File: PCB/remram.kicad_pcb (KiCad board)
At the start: 4 copper layers, 140 x 104 mm, 248 parts, among them J1 4DB-P108-06, J10 Conn_02x13_Odd_Even, J11 70543-0001, J12 70543-0002, J13 70543-0002, J14 70543-0002, J15 70543-0001, J16 70543-0002, J17 70543-0002, J18 70543-0002, J19 70543-0001, J2 039531-1002, J20 70543-0003, J21 70543-0003, J22 70543-0003, J23 70543-0003, J3 70543-0003, J4 67068-8000, J5 Conn_02x05, J6 Conn_02x05, J7 70543-0002, J8 70543-0002, J9 62201021121, Q1 PMV50EPEA, Q2 PSMN1R2-30YLC,115, Q3 BUK9840-55, Q4 PSMN1R2-30YLC,115, Q5 BUK9840-55, Q6 PMV50EPEA, SW1 OS102011MA1QN1, SW2 PTS645VL39-2, U1 TPS54308, U2 AP2112K-3.3TRG1, U3 ADUM4160, U4 STM32F765VIT6, U5 TMC2130-TA, U6 TMC2130-TA, U7 TMC2130-TA, U8 TMC2130-TA, Y1 TSX-3225 24.0000MF15X-AC3

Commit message: Made small cosmetic changes
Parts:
- added REF**: OSHW-Logo2_14.6x12mm_SilkScreen, Symbol:OSHW-Logo2_14.6x12mm_SilkScreen, F.Cu at (69.5, 76.2)
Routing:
- net /MCU/PWM_HEAT: track 76.3 -> 74.3 mm

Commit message: Fix minor cosmetic issues
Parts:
- moved C14 7.55 mm to (177.7, 93.8)
- moved C13 5.45 mm to (184.2, 92.8)
- moved D4 0.40 mm to (175.2, 118.0)
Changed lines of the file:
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@@
   (module custom-footprints:S8401-46 (layer F.Cu)
     (at 140.6 101 90)
-    (fp_text reference BT1 (at 0 4 90) (layer F.SilkS)
+    (fp_text reference BT1 (at 12.55 0 180) (layer F.SilkS)
       (effects (font (size 1 1) (thickness 0.15)))
     )
@@
     (tags capacitor)
     (attr smd)
-    (fp_text reference C22 (at -3.082727 -0.640025 180) (layer F.SilkS)
+    (fp_text reference C22 (at -2.782727 0.009975 180) (layer F.SilkS)
       (effects (font (size 1 1) (thickness 0.15)))
     )
@@
     (tags capacitor)
     (attr smd)
-    (fp_text reference C21 (at 2.6 2.8 -180) (layer F.SilkS)
+    (fp_text reference C21 (at -2.3 1.3 -180) (layer F.SilkS)
       (effects (font (size 1 1) (thickness 0.15)))
     )
@@
     (tags capacitor)
     (attr smd)
-    (fp_text reference C20 (at -1.85 1.9) (layer F.SilkS)
+    (fp_text reference C20 (at 2.3 1.5) (layer F.SilkS)
       (effects (font (size 1 1) (thickness 0.15)))
     )
@@
     (tags resistor)
     (attr smd)
-    (fp_text reference R21 (at 0 2.2) (layer F.SilkS)
+    (fp_text reference R21 (at 0 -2.2) (layer F.SilkS)
       (effects (font (size 1 1) (thickness 0.15)))
     )
@@
     (tags diode)
     (attr smd)
-    (fp_text reference D10 (at -3.1 0.05) (layer F.SilkS)
+    (fp_text reference D10 (at 1.4 2.35) (layer F.SilkS)
       (effects (font (size 1 1) (thickness 0.15)))
     )
@@
   )
   (module Capacitor_SMD:C_1812_4532Metric (layer F.Cu)
-    (at 185.25 93.85 270)
+    (at 177.7 93.75 270)
     (descr "Capacitor SMD 1812 (4532 Metric), square (rectangular) end terminal, IPC_7351 nominal, (Body size source: https://www.nikhef.nl/pub/departments/mt/projects/detectorR_D/dtddice/ERJ2G.pdf), generated with kicad-footprint-generator")
     (tags capacitor)
@@
   )
   (module Capacitor_THT:CP_Radial_D6.3mm_P2.50mm (layer F.Cu)
-    (at 178.75 92.85 270)
+    (at 184.2 92.85 270)
     (descr "CP, Radial series, Radial, pin pitch=2.50mm, , diameter=6.3mm, Electrolytic Capacitor")
     (tags "CP Radial series Radial pin pitch 2.50mm  diameter 6.3mm Electrolytic Capacitor")
@@
   )
   (module Diode_SMD:D_SMA (layer F.Cu)
-    (at 175.6 118.05 270)
+    (at 175.2 118.05 270)
     (descr "Diode SMA (DO-214AC)")
     (tags "Diode SMA (DO-214AC)")
@@
     (zone_connect 2)
     (attr smd)
-    (fp_text reference D2 (at -2.2 -0.03) (layer F.SilkS)
+    (fp_text reference D2 (at 2.25 0) (layer F.SilkS)
       (effects (font (size 1 1) (thickness 0.15)))
     )
@@
     (effects (font (size 1.5 1.5) (thickness 0.3)))
   )
-  (gr_text EXT-3 (at 137.2 117.75) (layer F.SilkS)
+  (gr_text EXT-3 (at 137.2 117.3) (layer F.SilkS)
     (effects (font (size 1.5 1.5) (thickness 0.3)))
   )
@@
       (pts
         (xy 202.2 63.25) (xy 202.2 66) (xy 187.45 66) (xy 187.45 64.75) (xy 173.45 64.75)
-        (xy 173.45 53) (xy 186.7 53) (xy 186.7 60.5) (xy 202.2 60.5)
+        (xy 173.45 53) (xy 186.7 53) (xy 186.7 57.25) (xy 202.2 57.25)
       )
     )

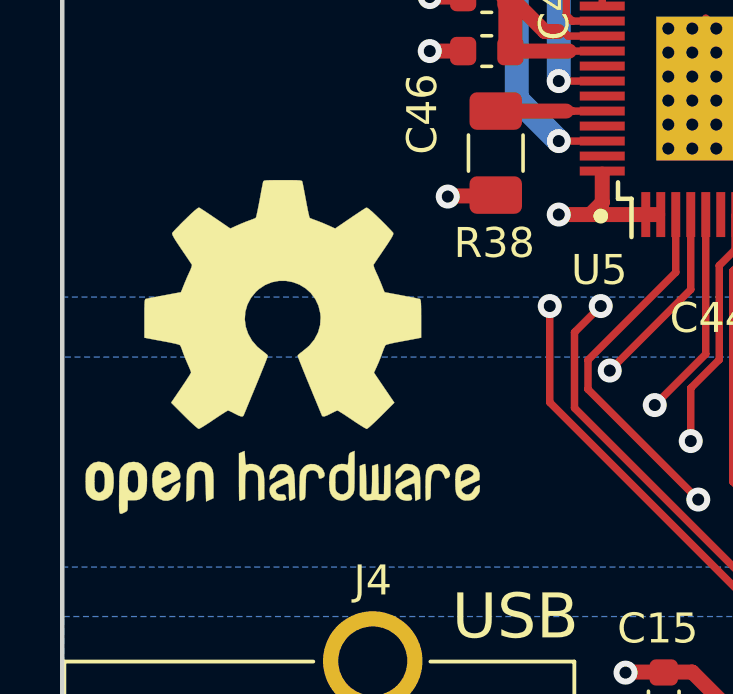
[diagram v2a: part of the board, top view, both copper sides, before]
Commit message: Revert back to IRLML6401 for battery protection
I reverted back to use the IRLML, since the gate-source threshhold
coltage for the other P MOSFET was not low enough to always work
inside the battery voltage.
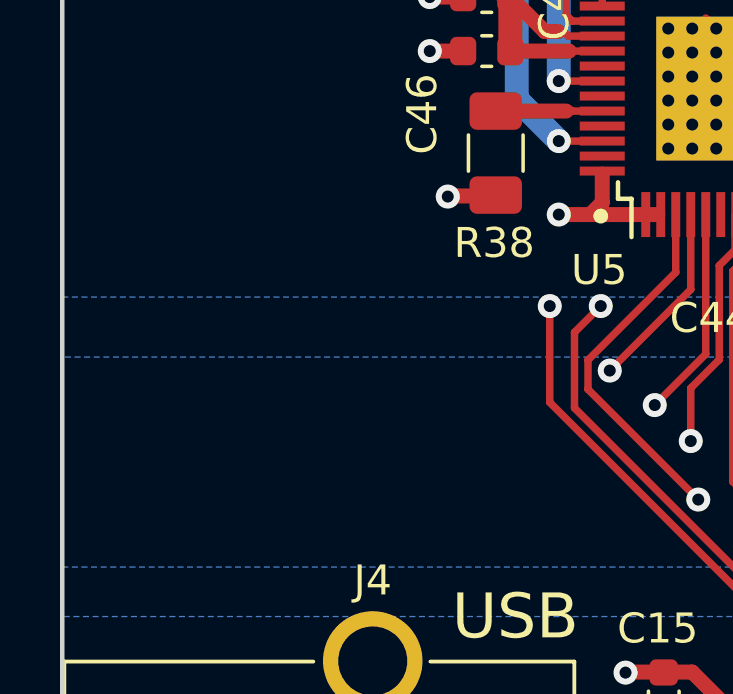
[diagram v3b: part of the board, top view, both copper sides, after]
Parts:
- removed REF**: OSHW-Logo2_14.6x12mm_SilkScreen, Symbol:OSHW-Logo2_14.6x12mm_SilkScreen
- Q6: value PMV50EPEA -> IRLML6401

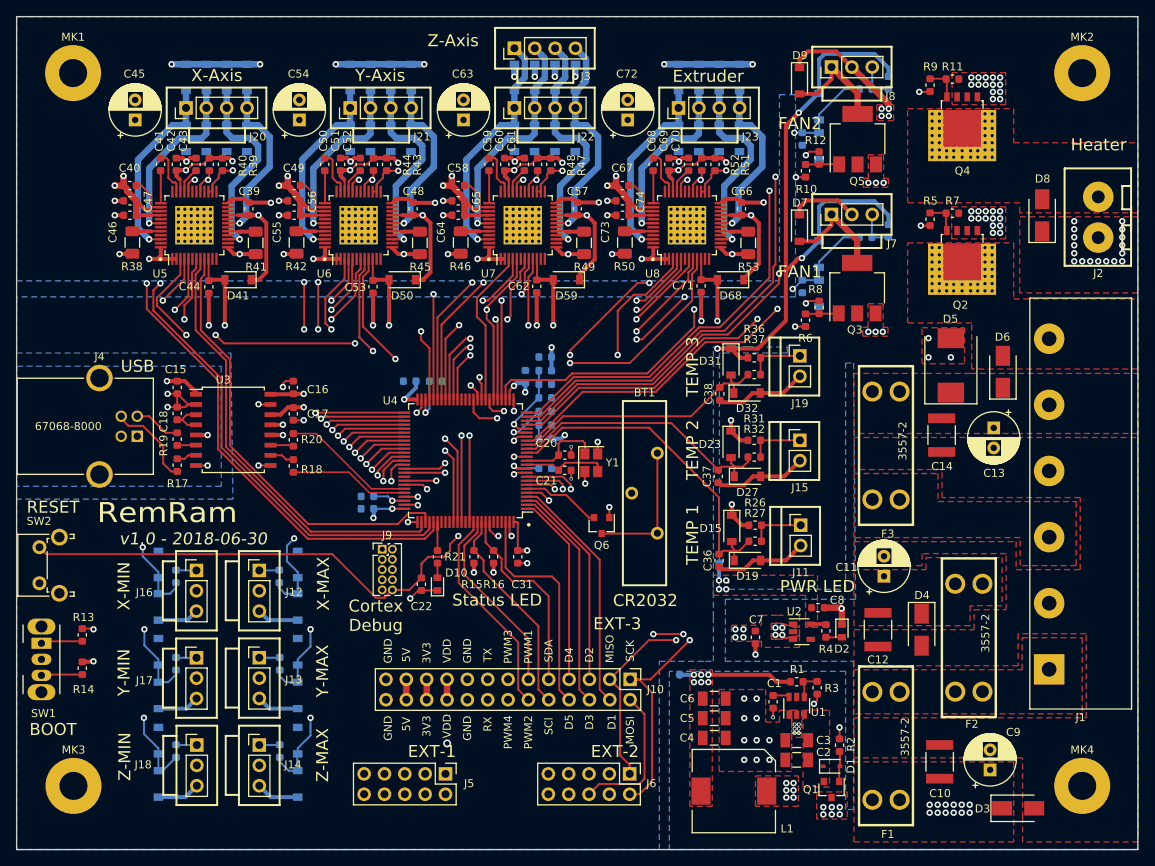
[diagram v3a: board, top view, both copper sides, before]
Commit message: Add compability for TPS54302
Since the TPS54308 is often not available, we added the
option to also use the TPS54038. This commit added a lot
of components and changed the CSV.
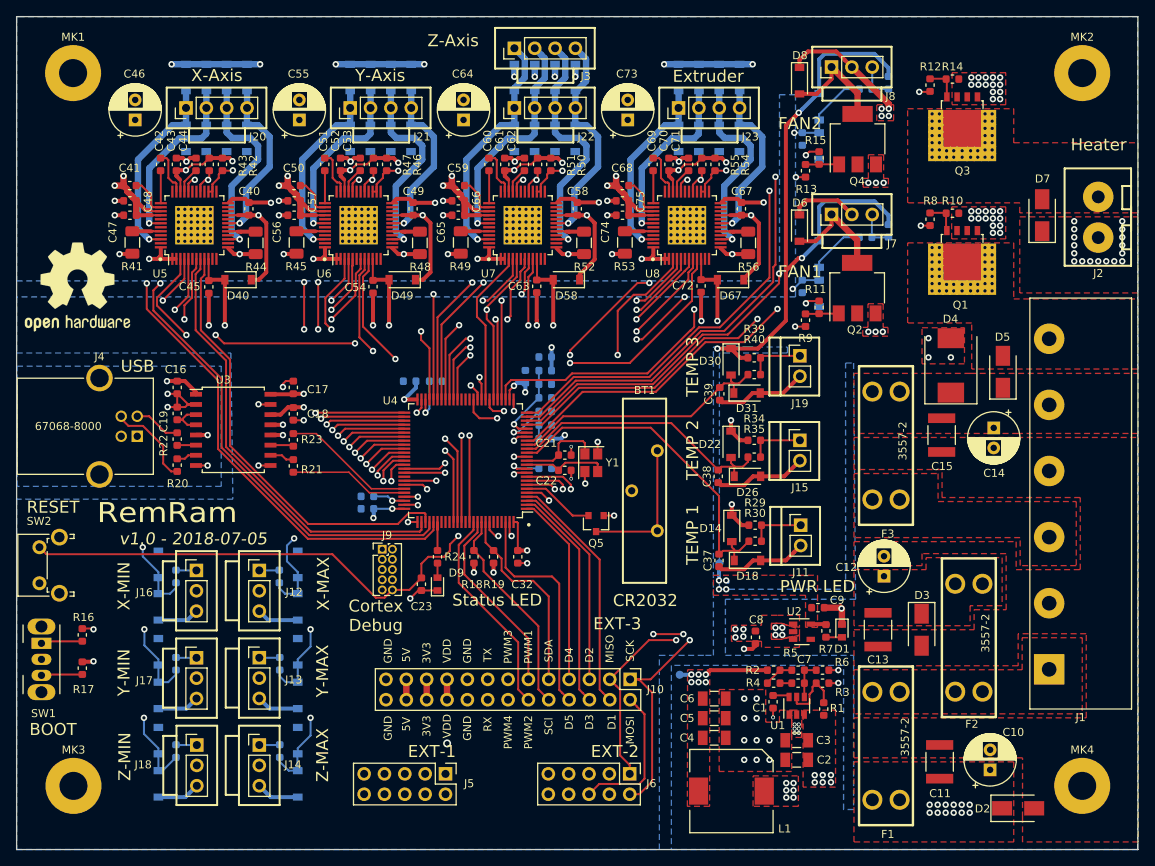
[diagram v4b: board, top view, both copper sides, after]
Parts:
- removed the D1 at (163.9, 135.1)
- removed the Q1 at (163.9, 138.0)
- added C7: 75pF, Capacitor_SMD:C_0603_1608Metric, F.Cu at (159.8, 124.7)
- added R1: 511k, Resistor_SMD:R_0603_1608Metric, F.Cu at (163.0, 128.0)
- added R3: 105k, Resistor_SMD:R_0603_1608Metric, F.Cu at (162.8, 124.7)
- added R4: 2k, Resistor_SMD:R_0603_1608Metric, F.Cu at (156.7, 124.7)
- added REF**: OSHW-Logo2_14.6x12mm_SilkScreen, Symbol:OSHW-Logo2_14.6x12mm_SilkScreen, F.Cu at (69.8, 75.2)
- BT1: value VBH2032-1 -> S8401-46
- R2: value 100k -> 49.9
- R6: renamed from R3; value 13,7k -> 13.3k
- moved R2 12.5 mm to (156.7, 123.1), turned to 0 degrees
- moved R6 2.30 mm to (162.8, 123.1), turned to 0 degrees
- moved R5 1.46 mm to (159.8, 123.1)
- moved Q5 0.74 mm to (134.6, 104.8)
- moved L1 0.30 mm to (151.4, 138.2)
- moved BT1 0.30 mm to (140.6, 100.7)
- renumbered C9 to C10, C10 to C11, C11 to C12, C12 to C13, C13 to C14, C14 to C15, C15 to C16, C16 to C17, C17 to C18, C18 to C19, C19 to C20, C20 to C21, C21 to C22, C22 to C23, C23 to C24, C24 to C25, C25 to C26, C26 to C27, C27 to C28, C28 to C29, C29 to C30, C30 to C31, C31 to C32, C32 to C33, C33 to C34, C34 to C35, C35 to C36, C36 to C37, C37 to C38, C38 to C39, C39 to C40, C40 to C41, C41 to C42, C42 to C43, C43 to C44, C44 to C45, C45 to C46, C46 to C47, C47 to C48, C48 to C49, C49 to C50, C50 to C51, C51 to C52, C52 to C53, C53 to C54, C54 to C55, C55 to C56, C56 to C57, C57 to C58, C58 to C59, C59 to C60, C60 to C61, C61 to C62, C62 to C63, C63 to C64, C64 to C65, C65 to C66, C66 to C67, C67 to C68, C68 to C69, C69 to C70, C70 to C71, C71 to C72, C72 to C73, C73 to C74, C74 to C75, C7 to C8, C8 to C9, D2 to D1, D11 to D10, D12 to D11, D13 to D12, D14 to D13, D15 to D14, D16 to D15, D17 to D16, D18 to D17, D19 to D18, D20 to D19, D3 to D2, D21 to D20, D22 to D21, D23 to D22, D24 to D23, D25 to D24, D26 to D25, D27 to D26, D28 to D27, D29 to D28, D30 to D29, D4 to D3, D31 to D30, D32 to D31, D33 to D32, D34 to D33, D35 to D34, D36 to D35, D37 to D36, D38 to D37, D39 to D38, D40 to D39, D5 to D4, D41 to D40, D42 to D41, D43 to D42, D44 to D43, D45 to D44, D46 to D45, D47 to D46, D48 to D47, D49 to D48, D50 to D49, D6 to D5, D51 to D50, D52 to D51, D53 to D52, D54 to D53, D55 to D54, D56 to D55, D57 to D56, D58 to D57, D59 to D58, D60 to D59, D7 to D6, D61 to D60, D62 to D61, D63 to D62, D64 to D63, D65 to D64, D66 to D65, D67 to D66, D68 to D67, D8 to D7, D9 to D8, D10 to D9, Q2 to Q1, Q3 to Q2, Q4 to Q3, Q5 to Q4, Q6 to Q5, R7 to R10, R8 to R11, R9 to R12, R10 to R13, R11 to R14, R12 to R15, R13 to R16, R14 to R17, R15 to R18, R16 to R19, R17 to R20, R18 to R21, R19 to R22, R20 to R23, R21 to R24, R22 to R25, R23 to R26, R24 to R27, R25 to R28, R26 to R29, R27 to R30, R28 to R31, R29 to R32, R30 to R33, R31 to R34, R32 to R35, R33 to R36, R34 to R37, R35 to R38, R36 to R39, R37 to R40, R38 to R41, R39 to R42, R40 to R43, R41 to R44, R42 to R45, R43 to R46, R44 to R47, R45 to R48, R46 to R49, R1 to R5, R47 to R50, R48 to R51, R49 to R52, R50 to R53, R51 to R54, R52 to R55, R53 to R56, R4 to R7, R5 to R8, R6 to R9
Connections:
- C2 pad 1: Net-(C2-Pad1) -> VDD_PWR
- C3 pad 1: Net-(C2-Pad1) -> VDD_PWR
- R2 pad 1: Net-(D1-Pad2) (its old number) -> VDD5V
- R2 pad 2: GND -> Net-(R2-Pad2)
- R5 pad 1: VDD5V -> Net-(R2-Pad2)
- U1 pad 3: Net-(C2-Pad1) -> VDD_PWR
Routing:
- net Net-(R1-Pad2): track 0.00 -> 8.13 mm
- net VDD5V: track 175.0 -> 168.8 mm
- net /MCU/SS_SD: track 73.4 -> 69.2 mm
- net Net-(D1-Pad2) (its old number): track 3.81 -> 0.00 mm
- net Net-(R2-Pad2): track 0.00 -> 3.75 mm
- net Net-(C7-Pad1): track 0.00 -> 1.48 mm
- net Net-(BT1-Pad2): track 17.0 -> 18.3 mm
- net Net-(C7-Pad2): track 3.73 -> 4.83 mm
- net Net-(Q5-Pad2): track 9.89 -> 9.09 mm
- removed copper zone on F.Cu, net Net-(C2-Pad1)
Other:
- board text added: "v1.0 - 2018-07-05"
- board text removed: "v1.0 - 2018-06-30"

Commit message: Add Schmitt Trigger for fan tachometer
The fan tachometer is too noise for the STM32F7 3.3V IO.
We need to add a Schmitt Trigger to have a better noise handling
and gain more low/high margin.

Also some minor silkscreen adjustments. Backward compatible
with v1.0.wq
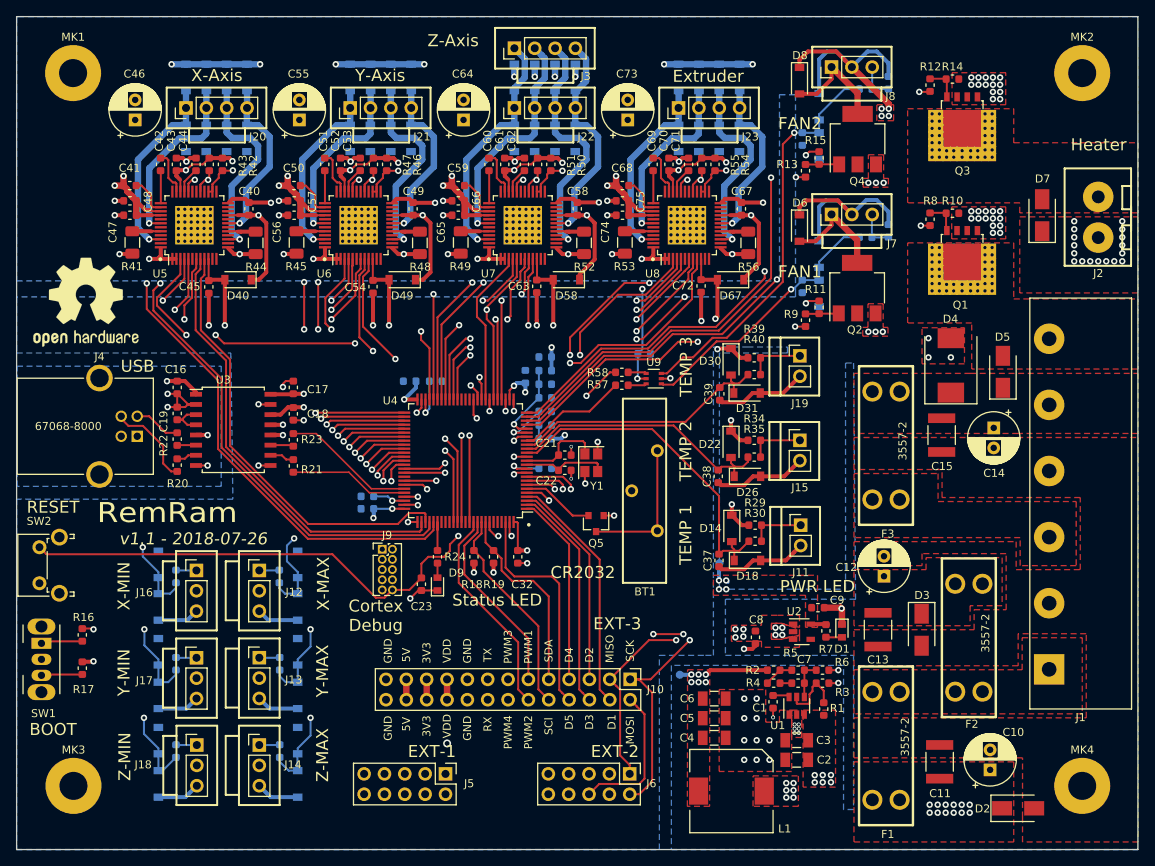
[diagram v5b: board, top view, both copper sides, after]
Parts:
- removed REF**: OSHW-Logo2_14.6x12mm_SilkScreen, Symbol:OSHW-Logo2_14.6x12mm_SilkScreen
- added C76: 100nF, Capacitor_SMD:C_0603_1608Metric, B.Cu at (140.6, 83.6)
- added LOGO1: Logo_Open_Hardware_Large, Symbol:OSHW-Logo2_14.6x12mm_SilkScreen, F.Cu at (70.8, 77.2)
- added R57: 1k, Resistor_SMD:R_0603_1608Metric, F.Cu at (137.8, 87.5)
- added R58: 1k, Resistor_SMD:R_0603_1608Metric, F.Cu at (137.8, 85.9)
- added U9: SN74LVC2G17DCKR, Package_TO_SOT_SMD:SOT-363_SC-70-6, F.Cu at (141.8, 86.7)
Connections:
- D10 pad 1: VDD3V3 -> VDD5V
- D12 pad 1: VDD3V3 -> VDD5V
- R25 pad 1: VDD3V3 -> VDD5V
- R27 pad 1: VDD3V3 -> VDD5V
- U4 pad 18: /MCU/FAN_SPEED1 -> /MCU/FAN_SPEED_1
- U4 pad 28: /MCU/FAN_SPEED2 -> /MCU/FAN_SPEED_2
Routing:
- net VDD3V3: track 228.4 -> 153.4 mm, vias 29 -> 27
- net VDD5V: track 168.8 -> 215.7 mm, vias 22 -> 24
- net /MCU/FAN_SPEED1: track 53.7 -> 34.2 mm, vias 2 -> 1
- net /MCU/FAN_SPEED2: track 69.5 -> 50.8 mm, vias 2 -> 1
- net /MCU/FAN_SPEED_2: track 0.00 -> 17.2 mm, vias 0 -> 2
- net /MCU/FAN_SPEED_1: track 0.00 -> 14.8 mm
- net /MCU/PWM_HEAT: track 74.3 -> 69.9 mm
- net Net-(R57-Pad1): track 0.00 -> 2.31 mm
- net Net-(R58-Pad1): track 0.00 -> 2.30 mm
- net GND: track 194.2 -> 195.2 mm, vias 111 -> 112
- net /Motor E/EN: track 55.7 -> 56.6 mm
- net /Motor E/SS: track 35.8 -> 35.0 mm
- net /MCU/PWM_FAN1: track 40.7 -> 39.9 mm
- net /MCU/PWM_BED: track 61.2 -> 60.5 mm
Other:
- board text added: "v1.1 - 2018-07-26"
- board text removed: "v1.0 - 2018-07-05"

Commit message: Change tachometer resistors to 4.7k and update BOM
To better filter the tachometer signal, we had to increase the
reistors of the tachometer RC filter and PU to 4.7k.

This commit also updates the BOM for all changed since v1.0.wq
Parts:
- R25, R26, R27, R28: value 1k -> 4.7k
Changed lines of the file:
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@@
       (effects (font (size 1 1) (thickness 0.15)) (justify mirror))
     )
-    (fp_text value 1k (at 0 -1.43 270) (layer B.Fab)
+    (fp_text value 4.7k (at 0 -1.43 270) (layer B.Fab)
       (effects (font (size 1 1) (thickness 0.15)) (justify mirror))
     )
@@
       (effects (font (size 1 1) (thickness 0.15)) (justify mirror))
     )
-    (fp_text value 1k (at 0 -1.43 180) (layer B.Fab)
+    (fp_text value 4.7k (at 0 -1.43 180) (layer B.Fab)
       (effects (font (size 1 1) (thickness 0.15)) (justify mirror))
     )
@@
       (effects (font (size 1 1) (thickness 0.15)) (justify mirror))
     )
-    (fp_text value 1k (at 0 -1.43 270) (layer B.Fab)
+    (fp_text value 4.7k (at 0 -1.43 270) (layer B.Fab)
       (effects (font (size 1 1) (thickness 0.15)) (justify mirror))
     )
@@
       (effects (font (size 1 1) (thickness 0.15)) (justify mirror))
     )
-    (fp_text value 1k (at 0 -1.43 180) (layer B.Fab)
-      (effects (font (size 1 1) (thickness 0.15)) (justify mirror))
-    )
+    (fp_text value 4.7k (at 0 -1.43 180) (layer B.Fab)
+      (effects (font (size 1 1) (thickness 0.15)) (justify mirror))
+    )

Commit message: Switch BTN_ENC1 & BTN_ENC2
Simple cosmetic change. The connector has them switched.
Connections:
- J6 pad 3: /MCU/BTN_EN1 -> /MCU/BTN_EN2
- J6 pad 5: /MCU/BTN_EN2 -> /MCU/BTN_EN1
- U4 pad 8: /MCU/BTN_EN2 -> /MCU/BTN_EN1
- U4 pad 9: /MCU/BTN_EN1 -> /MCU/BTN_EN2
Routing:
- net /MCU/BTN_EN2: track 43.3 -> 45.1 mm
- net /MCU/BTN_EN1: track 45.1 -> 43.3 mm
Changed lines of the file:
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@@
       (net 68 /MCU/SCK))
     (pad 3 thru_hole oval (at 0 2.54 270) (size 1.7 1.7) (drill 1) (layers *.Cu *.Mask)
-      (net 80 /MCU/BTN_EN1))
+      (net 79 /MCU/BTN_EN2))
     (pad 4 thru_hole oval (at 2.54 2.54 270) (size 1.7 1.7) (drill 1) (layers *.Cu *.Mask)
       (net 69 /MCU/SS_SD))
     (pad 5 thru_hole oval (at 0 5.08 270) (size 1.7 1.7) (drill 1) (layers *.Cu *.Mask)
-      (net 79 /MCU/BTN_EN2))
+      (net 80 /MCU/BTN_EN1))
     (pad 6 thru_hole oval (at 2.54 5.08 270) (size 1.7 1.7) (drill 1) (layers *.Cu *.Mask)
       (net 143 /MCU/MOSI))
@@
       (net 70 /MCU/SD_CARD_DET))
     (pad 8 smd rect (at -7.65 -2.5 180) (size 1.5 0.3) (layers F.Cu F.Paste F.Mask)
-      (net 79 /MCU/BTN_EN2))
-    (pad 9 smd rect (at -7.65 -2 180) (size 1.5 0.3) (layers F.Cu F.Paste F.Mask)
       (net 80 /MCU/BTN_EN1))
+    (pad 9 smd rect (at -7.65 -2 180) (size 1.5 0.3) (layers F.Cu F.Paste F.Mask)
+      (net 79 /MCU/BTN_EN2))
     (pad 10 smd rect (at -7.65 -1.5 180) (size 1.5 0.3) (layers F.Cu F.Paste F.Mask)
       (net 1 GND))
@@
   (segment (start 97.3 132.85) (end 98.9 131.25) (width 0.25) (layer B.Cu) (net 78))
   (segment (start 97.3 133.55) (end 97.3 132.85) (width 0.25) (layer B.Cu) (net 78) (status 10))
-  (via (at 130.4 100.5) (size 0.8) (drill 0.4) (layers F.Cu B.Cu) (net 79))
-  (segment (start 130.4 99.934315) (end 130.4 100.5) (width 0.25) (layer F.Cu) (net 79))
-  (segment (start 125.9 99.45) (end 129.915685 99.45) (width 0.25) (layer F.Cu) (net 79) (status 10))
-  (segment (start 129.915685 99.45) (end 130.4 99.934315) (width 0.25) (layer F.Cu) (net 79))
-  (segment (start 133.67 130.007) (end 133.67 136.05) (width 0.25) (layer In1.Cu) (net 79) (status 20))
-  (segment (start 135 128.677) (end 133.67 130.007) (width 0.25) (layer In1.Cu) (net 79))
-  (segment (start 135 106.6) (end 135 128.677) (width 0.25) (layer In1.Cu) (net 79))
-  (segment (start 130.4 100.5) (end 130.4 102) (width 0.25) (layer In1.Cu) (net 79))
-  (segment (start 130.4 102) (end 135 106.6) (width 0.25) (layer In1.Cu) (net 79))
-  (via (at 131.400013 100.5) (size 0.8) (drill 0.4) (layers F.Cu B.Cu) (net 80))
-  (segment (start 125.9 98.95) (end 130.415698 98.95) (width 0.25) (layer F.Cu) (net 80) (status 10))
-  (segment (start 130.415698 98.95) (end 131.400013 99.934315) (width 0.25) (layer F.Cu) (net 80))
-  (segment (start 131.400013 99.934315) (end 131.400013 100.5) (width 0.25) (layer F.Cu) (net 80))
-  (segment (start 137.55 106.649987) (end 131.400013 100.5) (width 0.25) (layer In1.Cu) (net 80))
-  (segment (start 136.21 136.05) (end 137.55 134.71) (width 0.25) (layer In1.Cu) (net 80) (status 10))
-  (segment (start 137.55 134.71) (end 137.55 106.649987) (width 0.25) (layer In1.Cu) (net 80))
+  (via (at 130.4 100.5) (size 0.8) (drill 0.4) (layers F.Cu B.Cu) (net 80))
+  (segment (start 130.4 99.934315) (end 130.4 100.5) (width 0.25) (layer F.Cu) (net 80))
+  (segment (start 125.9 99.45) (end 129.915685 99.45) (width 0.25) (layer F.Cu) (net 80) (status 10))
+  (segment (start 129.915685 99.45) (end 130.4 99.934315) (width 0.25) (layer F.Cu) (net 80))
+  (segment (start 133.67 130.007) (end 133.67 136.05) (width 0.25) (layer In1.Cu) (net 80) (status 20))
+  (segment (start 135 128.677) (end 133.67 130.007) (width 0.25) (layer In1.Cu) (net 80))
+  (segment (start 135 106.6) (end 135 128.677) (width 0.25) (layer In1.Cu) (net 80))
+  (segment (start 130.4 100.5) (end 130.4 102) (width 0.25) (layer In1.Cu) (net 80))
+  (segment (start 130.4 102) (end 135 106.6) (width 0.25) (layer In1.Cu) (net 80))
+  (via (at 131.400013 100.5) (size 0.8) (drill 0.4) (layers F.Cu B.Cu) (net 79))
+  (segment (start 125.9 98.95) (end 130.415698 98.95) (width 0.25) (layer F.Cu) (net 79) (status 10))
+  (segment (start 130.415698 98.95) (end 131.400013 99.934315) (width 0.25) (layer F.Cu) (net 79))
+  (segment (start 131.400013 99.934315) (end 131.400013 100.5) (width 0.25) (layer F.Cu) (net 79))
+  (segment (start 137.55 106.649987) (end 131.400013 100.5) (width 0.25) (layer In1.Cu) (net 79))
+  (segment (start 136.21 136.05) (end 137.55 134.71) (width 0.25) (layer In1.Cu) (net 79) (status 10))
+  (segment (start 137.55 134.71) (end 137.55 106.649987) (width 0.25) (layer In1.Cu) (net 79))
   (via (at 108.985181 99.500536) (size 0.8) (drill 0.4) (layers F.Cu B.Cu) (net 81))
   (segment (start 108.985181 98.064819) (end 108.985181 99.500536) (width 0.25) (layer F.Cu) (net 81))
